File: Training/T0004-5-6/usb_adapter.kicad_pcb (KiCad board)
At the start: 2 copper layers, 50.8 x 25.4 mm, 23 parts, among them J1 modular8_rev3_comms_out, P1 USB_OTG, U1 FT231X, U2 TE_1825058-1

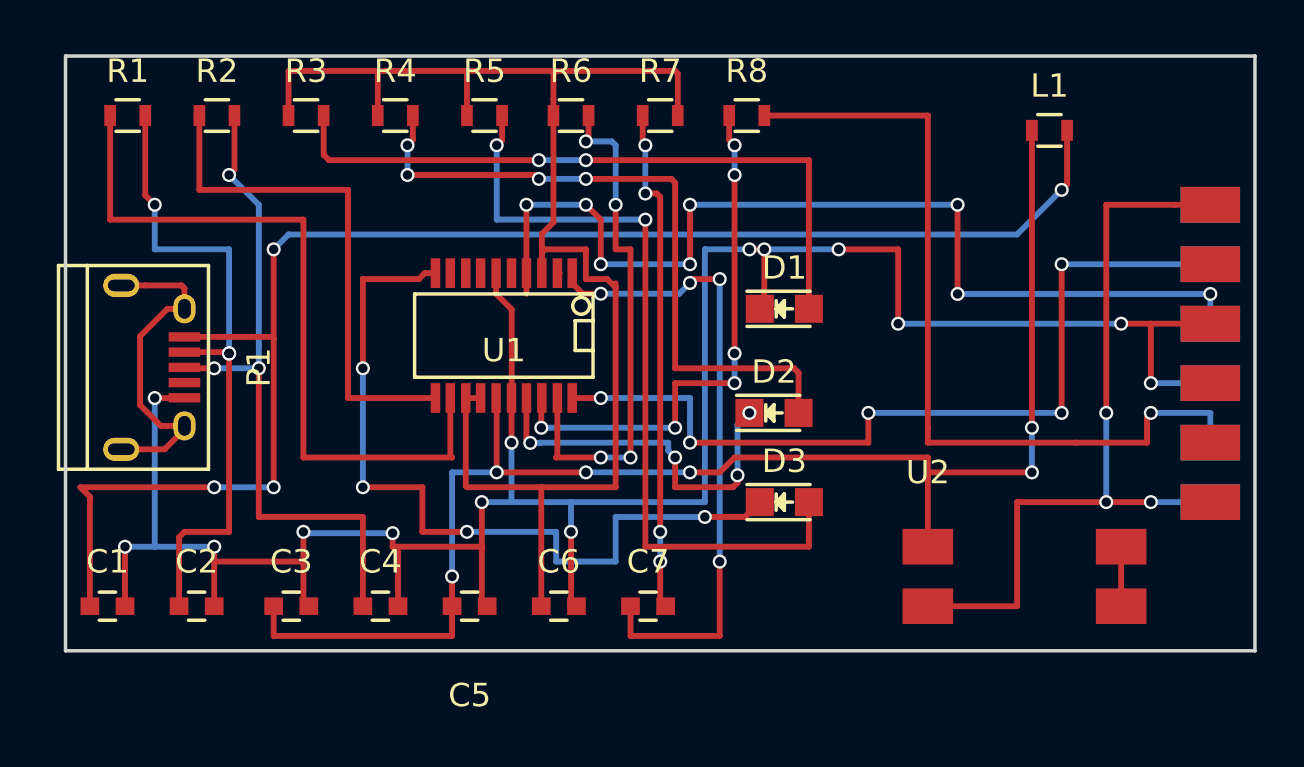
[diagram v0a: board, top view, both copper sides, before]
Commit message: fixed switch footprint
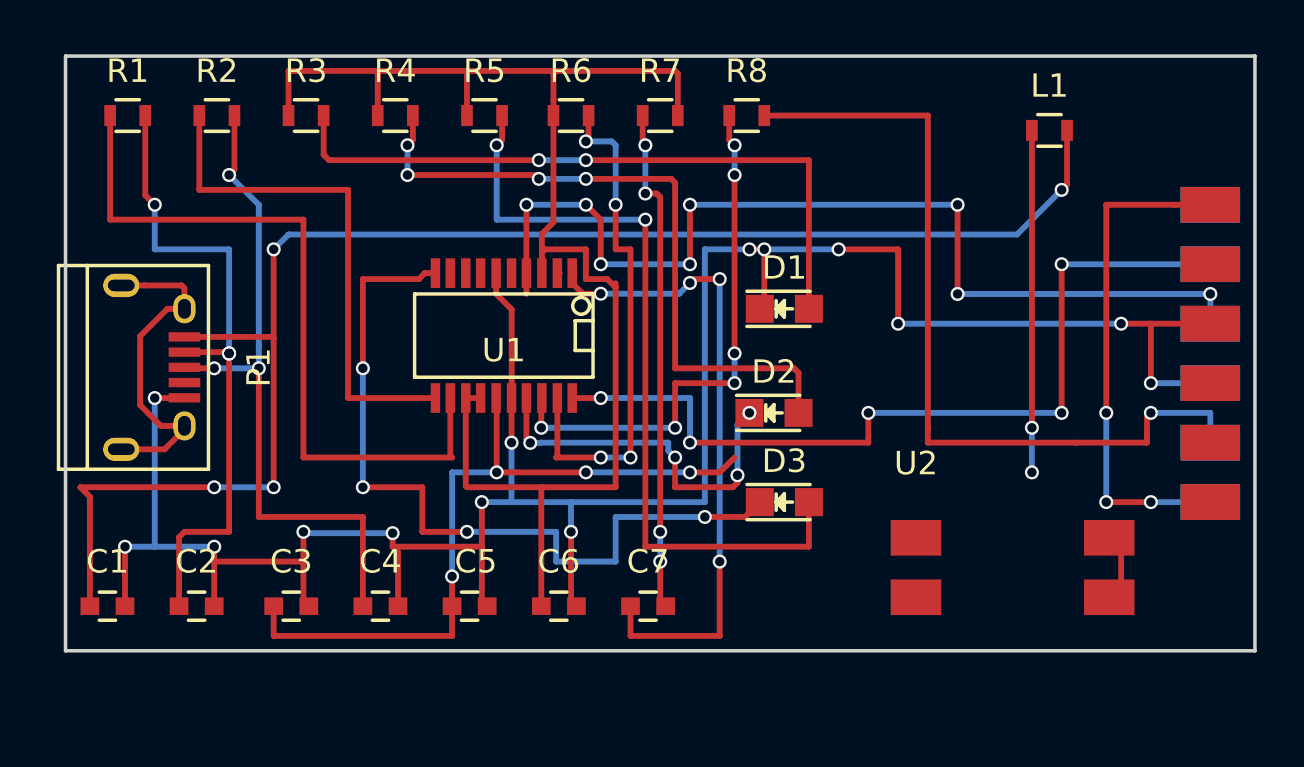
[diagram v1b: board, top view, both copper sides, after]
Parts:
- U1: value FT231X -> FT231XS
- moved U2 0.64 mm to (163.3, 122.2)
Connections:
- U2 pad 1: +5V -> /POWER_OUT
- U2 pad 2: /POWER_OUT -> Net-(J1-Pad7)
- U2 pad 3: (no net) -> /PROGRAM
- U2 pad 4: (no net) -> +5V
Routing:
- net +5V: track 62.8 -> 48.5 mm
- net /POWER_OUT: track 33.7 -> 21.6 mm
- net (no net): track 2.54 -> 0.00 mm
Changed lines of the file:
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@@
-(kicad_pcb (version 4) (host pcbnew "(2015-10-02 BZR 6241)-product")
+(kicad_pcb (version 4) (host pcbnew 4.0.0-rc1-stable)
   (general
-    (links 48)
-    (no_connects 48)
-    (area 124.59246 101.115 180.68 127.34)
+    (links 50)
+    (no_connects 5)
+    (area 126.924999 101.524999 177.875001 127.075001)
     (thickness 1.6)
     (drawings 4)
-    (tracks 374)
+    (tracks 366)
     (zones 0)
     (modules 23)
@@
     (46 B.CrtYd user)
     (47 F.CrtYd user)
-    (48 B.Fab user)
-    (49 F.Fab user)
+    (48 B.Fab user hide)
+    (49 F.Fab user hide)
   )
   (setup
@@
     (pad_to_mask_clearance 0.2)
     (aux_axis_origin 0 0)
-    (visible_elements FFFFFF7F)
+    (visible_elements 7FFFFFFF)
     (pcbplotparams
       (layerselection 0x00030_80000001)
@@
     (tags "capacitor 0603")
     (attr smd)
-    (fp_text reference C5 (at 0 3.81) (layer F.SilkS)
+    (fp_text reference C5 (at 0.266 -1.905) (layer F.SilkS)
       (effects (font (size 1 1) (thickness 0.15)))
     )
@@
       (effects (font (size 1 1) (thickness 0.15)))
     )
-    (fp_text value FT231X (at 0 0.635 180) (layer F.Fab)
+    (fp_text value FT231XS (at 0 0.635 180) (layer F.Fab)
       (effects (font (size 1 1) (thickness 0.15)))
     )
@@
   )
   (module open_robotics:DIPSWITCH_SMT_ALCO_2CCT (layer F.Cu)
-    (at 163.83 122.555)
+    (at 163.322 122.174)
     (fp_text reference U2 (at 0 -3.175) (layer F.SilkS)
       (effects (font (size 1 1) (thickness 0.15)))
@@
     (fp_line (start -1.905 -2.54) (end -1.905 5.08) (layer F.CrtYd) (width 0.15))
     (pad 1 smd rect (at 0 0) (size 2.159 1.524) (layers F.Cu F.Paste F.Mask)
+      (net 14 /POWER_OUT))
+    (pad 2 smd rect (at 0 2.54) (size 2.159 1.524) (layers F.Cu F.Paste F.Mask)
+      (net 16 "Net-(J1-Pad7)"))
+    (pad 3 smd rect (at 8.255 2.54) (size 2.159 1.524) (layers F.Cu F.Paste F.Mask)
+      (net 8 /PROGRAM))
+    (pad 4 smd rect (at 8.255 0) (size 2.159 1.524) (layers F.Cu F.Paste F.Mask)
       (net 4 +5V))
-    (pad 2 smd rect (at 0 2.54) (size 2.159 1.524) (layers F.Cu F.Paste F.Mask)
-      (net 14 /POWER_OUT))
-    (pad 3 smd rect (at 8.255 2.54) (size 2.159 1.524) (layers F.Cu F.Paste F.Mask))
-    (pad 4 smd rect (at 8.255 0) (size 2.159 1.524) (layers F.Cu F.Paste F.Mask))
   )
   (gr_line (start 127 127) (end 127 101.6) (angle 90) (layer Edge.Cuts) (width 0.15))
@@
   (gr_line (start 177.8 101.6) (end 177.8 127) (angle 90) (layer Edge.Cuts) (width 0.15))
   (gr_line (start 127 101.6) (end 177.8 101.6) (angle 90) (layer Edge.Cuts) (width 0.15))
-  (segment (start 172.085 122.555) (end 172.085 125.095) (width 0.25) (layer F.Cu) (net 0))
   (segment (start 127.635 120.015) (end 128.04 120.42) (width 0.25) (layer F.Cu) (net 1))
   (segment (start 128.04 120.42) (end 128.04 125.095) (width 0.25) (layer F.Cu) (net 1))
@@
   (segment (start 130.405 107.545) (end 130.81 107.95) (width 0.25) (layer F.Cu) (net 3))
   (via (at 130.81 107.95) (size 0.6) (drill 0.4) (layers F.Cu B.Cu) (net 3))
-  (segment (start 163.83 119.38) (end 163.83 119.632562) (width 0.25) (layer F.Cu) (net 4))
-  (segment (start 163.83 119.632562) (end 163.83 122.555) (width 0.25) (layer F.Cu) (net 4))
-  (segment (start 163.83 118.745) (end 163.83 119.632562) (width 0.25) (layer F.Cu) (net 4))
-  (segment (start 155.575 118.745) (end 163.83 118.745) (width 0.25) (layer F.Cu) (net 4))
+  (segment (start 172.085 122.555) (end 172.085 125.095) (width 0.25) (layer F.Cu) (net 4))
   (segment (start 154.94 119.38) (end 155.575 118.745) (width 0.25) (layer F.Cu) (net 4))
   (segment (start 153.67 119.38) (end 154.94 119.38) (width 0.25) (layer F.Cu) (net 4))
@@
   (segment (start 143.51 125.095) (end 143.51 123.825) (width 0.25) (layer F.Cu) (net 4))
   (via (at 143.51 123.825) (size 0.6) (drill 0.4) (layers F.Cu B.Cu) (net 4))
-  (segment (start 168.275 119.38) (end 163.83 119.38) (width 0.25) (layer F.Cu) (net 4))
   (segment (start 168.275 117.475) (end 168.275 119.38) (width 0.25) (layer B.Cu) (net 4))
   (via (at 168.275 119.38) (size 0.6) (drill 0.4) (layers F.Cu B.Cu) (net 4))
@@
   (segment (start 171.45 120.65) (end 173.355 120.65) (width 0.25) (layer F.Cu) (net 14))
   (via (at 173.355 120.65) (size 0.6) (drill 0.4) (layers F.Cu B.Cu) (net 14))
-  (segment (start 167.64 125.095) (end 163.83 125.095) (width 0.25) (layer F.Cu) (net 14))
-  (segment (start 167.64 120.65) (end 167.64 125.095) (width 0.25) (layer F.Cu) (net 14))
-  (segment (start 171.45 120.65) (end 167.64 120.65) (width 0.25) (layer F.Cu) (net 14))
   (segment (start 171.45 116.84) (end 171.45 120.65) (width 0.25) (layer B.Cu) (net 14))
   (via (at 171.45 120.65) (size 0.6) (drill 0.4) (layers F.Cu B.Cu) (net 14))

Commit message: finished
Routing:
- net Net-(J1-Pad7): track 0.00 -> 27.0 mm, vias 0 -> 2
- net /PROGRAM: track 21.6 -> 43.4 mm, vias 4 -> 6
- net +5V: track 48.5 -> 68.1 mm, vias 6 -> 9
- net /POWER_OUT: track 21.6 -> 30.3 mm
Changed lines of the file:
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@@
-(kicad_pcb (version 4) (host pcbnew 4.0.0-rc1-stable)
+(kicad_pcb (version 4) (host pcbnew "(2015-10-02 BZR 6241)-product")
   (general
     (links 50)
     (no_connects 5)
-    (area 126.924999 101.524999 177.875001 127.075001)
+    (area 124.59246 101.115 180.68 127.97)
     (thickness 1.6)
     (drawings 4)
-    (tracks 366)
+    (tracks 400)
     (zones 0)
     (modules 23)
@@
   (segment (start 130.405 107.545) (end 130.81 107.95) (width 0.25) (layer F.Cu) (net 3))
   (via (at 130.81 107.95) (size 0.6) (drill 0.4) (layers F.Cu B.Cu) (net 3))
+  (segment (start 168.275 122.555) (end 171.196 122.555) (width 0.25) (layer F.Cu) (net 4))
+  (segment (start 171.196 122.555) (end 171.577 122.174) (width 0.25) (layer F.Cu) (net 4))
+  (segment (start 168.275 119.38) (end 168.275 122.555) (width 0.25) (layer B.Cu) (net 4))
+  (via (at 168.275 122.555) (size 0.6) (drill 0.4) (layers F.Cu B.Cu) (net 4))
+  (segment (start 156.845 119.38) (end 158.115 119.38) (width 0.25) (layer B.Cu) (net 4))
+  (segment (start 155.575 118.745) (end 156.21 118.745) (width 0.25) (layer F.Cu) (net 4))
+  (via (at 156.845 119.38) (size 0.6) (drill 0.4) (layers F.Cu B.Cu) (net 4))
+  (segment (start 156.21 118.745) (end 156.845 119.38) (width 0.25) (layer F.Cu) (net 4))
+  (segment (start 155.300839 119.019161) (end 155.575 118.745) (width 0.25) (layer F.Cu) (net 4))
+  (segment (start 154.94 119.38) (end 155.300839 119.019161) (width 0.25) (layer F.Cu) (net 4))
+  (segment (start 163.83 119.38) (end 158.115 119.38) (width 0.25) (layer B.Cu) (net 4))
+  (segment (start 168.275 119.38) (end 163.83 119.38) (width 0.25) (layer F.Cu) (net 4))
+  (via (at 163.83 119.38) (size 0.6) (drill 0.4) (layers F.Cu B.Cu) (net 4))
   (segment (start 172.085 122.555) (end 172.085 125.095) (width 0.25) (layer F.Cu) (net 4))
-  (segment (start 154.94 119.38) (end 155.575 118.745) (width 0.25) (layer F.Cu) (net 4))
   (segment (start 153.67 119.38) (end 154.94 119.38) (width 0.25) (layer F.Cu) (net 4))
   (segment (start 149.225 119.38) (end 153.67 119.38) (width 0.25) (layer B.Cu) (net 4))
@@
   (segment (start 151.13 126.365) (end 154.94 126.365) (width 0.25) (layer F.Cu) (net 7))
   (segment (start 151.13 125.095) (end 151.13 126.365) (width 0.25) (layer F.Cu) (net 7))
+  (segment (start 171.45 126.365) (end 171.45 124.841) (width 0.25) (layer F.Cu) (net 8))
+  (segment (start 171.45 124.841) (end 171.577 124.714) (width 0.25) (layer F.Cu) (net 8))
+  (segment (start 160.02 126.365) (end 171.45 126.365) (width 0.25) (layer B.Cu) (net 8))
+  (via (at 171.45 126.365) (size 0.6) (drill 0.4) (layers F.Cu B.Cu) (net 8))
+  (segment (start 160.02 125.095) (end 160.02 126.365) (width 0.25) (layer B.Cu) (net 8))
+  (segment (start 154.305 125.095) (end 160.02 125.095) (width 0.25) (layer B.Cu) (net 8))
+  (segment (start 152.63 125.095) (end 154.305 125.095) (width 0.25) (layer F.Cu) (net 8))
+  (via (at 154.305 125.095) (size 0.6) (drill 0.4) (layers F.Cu B.Cu) (net 8))
   (segment (start 152.4 123.19) (end 152.4 124.865) (width 0.25) (layer F.Cu) (net 8))
   (segment (start 152.4 124.865) (end 152.63 125.095) (width 0.25) (layer F.Cu) (net 8))
@@
   (segment (start 142.7988 110.871) (end 142.3456 110.871) (width 0.25) (layer F.Cu) (net 13))
   (segment (start 142.3456 110.871) (end 142.0916 111.125) (width 0.25) (layer F.Cu) (net 13))
+  (segment (start 164.846 122.174) (end 166.37 120.65) (width 0.25) (layer F.Cu) (net 14))
+  (segment (start 166.37 120.65) (end 171.45 120.65) (width 0.25) (layer F.Cu) (net 14))
+  (segment (start 163.322 122.174) (end 164.846 122.174) (width 0.25) (layer F.Cu) (net 14))
   (segment (start 173.355 120.65) (end 175.895 120.65) (width 0.25) (layer B.Cu) (net 14))
   (segment (start 171.45 120.65) (end 173.355 120.65) (width 0.25) (layer F.Cu) (net 14))
@@
   (segment (start 174.375 107.95) (end 171.45 107.95) (width 0.25) (layer F.Cu) (net 14))
   (segment (start 175.895 107.95) (end 174.375 107.95) (width 0.25) (layer F.Cu) (net 14))
+  (segment (start 163.195 114.3) (end 163.195 118.11141) (width 0.25) (layer F.Cu) (net 16))
+  (segment (start 163.195 118.11141) (end 160.655 120.65141) (width 0.25) (layer F.Cu) (net 16))
+  (segment (start 160.655 120.65141) (end 160.655 122.3645) (width 0.25) (layer F.Cu) (net 16))
+  (segment (start 160.655 122.3645) (end 163.0045 124.714) (width 0.25) (layer F.Cu) (net 16))
+  (segment (start 163.0045 124.714) (end 163.322 124.714) (width 0.25) (layer F.Cu) (net 16))
+  (segment (start 173.99 114.3) (end 163.195 114.3) (width 0.25) (layer B.Cu) (net 16))
+  (via (at 163.195 114.3) (size 0.6) (drill 0.4) (layers F.Cu B.Cu) (net 16))
+  (segment (start 175.895 114.3) (end 173.99 114.3) (width 0.25) (layer F.Cu) (net 16))
+  (via (at 173.99 114.3) (size 0.6) (drill 0.4) (layers F.Cu B.Cu) (net 16))
+  (segment (start 175.895 115.57) (end 175.895 114.3) (width 0.25) (layer F.Cu) (net 16))
+  (segment (start 163.322 124.714) (end 163.6395 124.714) (width 0.25) (layer F.Cu) (net 16))
   (segment (start 149.86 116.205) (end 148.6408 116.205) (width 0.25) (layer F.Cu) (net 20))
   (segment (start 153.67 116.205) (end 149.86 116.205) (width 0.25) (layer B.Cu) (net 20))

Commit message: generated gerbers
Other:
- board text added: "USB to serial Tiffany OpenRobotics.ca"
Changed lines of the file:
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@@
-(kicad_pcb (version 4) (host pcbnew "(2015-10-02 BZR 6241)-product")
+(kicad_pcb (version 4) (host pcbnew 4.0.0-rc1-stable)
   (general
     (links 50)
-    (no_connects 5)
+    (no_connects 0)
     (area 124.59246 101.115 180.68 127.97)
     (thickness 1.6)
-    (drawings 4)
+    (drawings 5)
     (tracks 400)
     (zones 0)
@@
     (visible_elements 7FFFFFFF)
     (pcbplotparams
-      (layerselection 0x00030_80000001)
-      (usegerberextensions false)
+      (layerselection 0x010f0_80000001)
+      (usegerberextensions true)
       (excludeedgelayer true)
       (linewidth 0.100000)
@@
       (outputformat 1)
       (mirror false)
-      (drillshape 1)
+      (drillshape 0)
       (scaleselection 1)
-      (outputdirectory ""))
+      (outputdirectory ../gerbers/Tiffany/))
   )
   (net 0 "")
@@
     )
   )
-  (module open_robotics:modular8_rev3_edge (layer F.Cu)
-    (at 175.895 113.03 270)
-    (fp_text reference J1 (at -3.81 -3.81 270) (layer F.SilkS) hide
-      (effects (font (size 1 1) (thickness 0.15)))
-    )
-    (fp_text value modular8_rev3_comms_out (at 1.27 -2.54 270) (layer F.Fab) hide
-      (effects (font (size 1 1) (thickness 0.15)))
-    )
-    (pad 1 smd rect (at -5.08 0 270) (size 1.524 2.54) (layers F.Cu F.Paste F.Mask)
-      (net 14 /POWER_OUT))
-    (pad 3 smd rect (at -2.54 0 270) (size 1.524 2.54) (layers F.Cu F.Paste F.Mask)
-      (net 15 "Net-(J1-Pad3)"))
-    (pad 5 smd rect (at 0 0 270) (size 1.524 2.54) (layers F.Cu F.Paste F.Mask)
-      (net 2 GND))
-    (pad 7 smd rect (at 2.54 0 270) (size 1.524 2.54) (layers F.Cu F.Paste F.Mask)
-      (net 16 "Net-(J1-Pad7)"))
-    (pad 9 smd rect (at 5.08 0 270) (size 1.524 2.54) (layers F.Cu F.Paste F.Mask)
-      (net 17 "Net-(J1-Pad9)"))
-    (pad 11 smd rect (at 7.62 0 270) (size 1.524 2.54) (layers F.Cu F.Paste F.Mask)
-      (net 18 "Net-(J1-Pad11)"))
-    (pad 2 smd rect (at -5.08 0 270) (size 1.524 2.54) (layers B.Cu F.Paste F.Mask)
-      (net 19 "Net-(J1-Pad2)"))
-    (pad 4 smd rect (at -2.54 0 270) (size 1.524 2.54) (layers B.Cu F.Paste F.Mask)
-      (net 20 /TX))
-    (pad 6 smd rect (at 0 0 270) (size 1.524 2.54) (layers B.Cu F.Paste F.Mask)
-      (net 21 /RX))
-    (pad 8 smd rect (at 2.54 0 270) (size 1.524 2.54) (layers B.Cu F.Paste F.Mask)
-      (net 2 GND))
-    (pad 10 smd rect (at 5.08 0 270) (size 1.524 2.54) (layers B.Cu F.Paste F.Mask)
-      (net 22 "Net-(J1-Pad10)"))
-    (pad 12 smd rect (at 7.62 0 270) (size 1.524 2.54) (layers B.Cu F.Paste F.Mask)
-      (net 14 /POWER_OUT))
-  )
   (module Resistors_SMD:R_0603 (layer F.Cu)
     (at 169.025 104.775)
@@
       (net 4 +5V))
   )
+  (module open_robotics:modular8_rev3_edge (layer F.Cu)
+    (at 175.895 113.03 270)
+    (fp_text reference J1 (at -3.81 -3.81 270) (layer F.SilkS) hide
+      (effects (font (size 1 1) (thickness 0.15)))
+    )
+    (fp_text value modular8_rev3_comms_out (at 1.27 -2.54 270) (layer F.Fab) hide
+      (effects (font (size 1 1) (thickness 0.15)))
+    )
+    (pad 1 smd rect (at -5.08 0 270) (size 1.524 2.54) (layers F.Cu F.Paste F.Mask)
+      (net 14 /POWER_OUT))
+    (pad 3 smd rect (at -2.54 0 270) (size 1.524 2.54) (layers F.Cu F.Paste F.Mask)
+      (net 15 "Net-(J1-Pad3)"))
+    (pad 5 smd rect (at 0 0 270) (size 1.524 2.54) (layers F.Cu F.Paste F.Mask)
+      (net 2 GND))
+    (pad 7 smd rect (at 2.54 0 270) (size 1.524 2.54) (layers F.Cu F.Paste F.Mask)
+      (net 16 "Net-(J1-Pad7)"))
+    (pad 9 smd rect (at 5.08 0 270) (size 1.524 2.54) (layers F.Cu F.Paste F.Mask)
+      (net 17 "Net-(J1-Pad9)"))
+    (pad 11 smd rect (at 7.62 0 270) (size 1.524 2.54) (layers F.Cu F.Paste F.Mask)
+      (net 18 "Net-(J1-Pad11)"))
+    (pad 2 smd rect (at -5.08 0 270) (size 1.524 2.54) (layers B.Cu B.Paste B.Mask)
+      (net 19 "Net-(J1-Pad2)"))
+    (pad 4 smd rect (at -2.54 0 270) (size 1.524 2.54) (layers B.Cu B.Paste B.Mask)
+      (net 20 /TX))
+    (pad 6 smd rect (at 0 0 270) (size 1.524 2.54) (layers B.Cu B.Paste B.Mask)
+      (net 21 /RX))
+    (pad 8 smd rect (at 2.54 0 270) (size 1.524 2.54) (layers B.Cu B.Paste B.Mask)
+      (net 2 GND))
+    (pad 10 smd rect (at 5.08 0 270) (size 1.524 2.54) (layers B.Cu B.Paste B.Mask)
+      (net 22 "Net-(J1-Pad10)"))
+    (pad 12 smd rect (at 7.62 0 270) (size 1.524 2.54) (layers B.Cu B.Paste B.Mask)
+      (net 14 /POWER_OUT))
+  )
+  (gr_text "USB to serial\nTiffany\nOpenRobotics.ca" (at 127.508 104.14 180) (layer B.SilkS)
+    (effects (font (size 1 1) (thickness 0.1)) (justify left mirror))
+  )
   (gr_line (start 127 127) (end 127 101.6) (angle 90) (layer Edge.Cuts) (width 0.15))
